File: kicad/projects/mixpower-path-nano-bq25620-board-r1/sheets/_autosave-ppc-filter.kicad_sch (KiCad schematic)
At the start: 5 parts, among them U4 TPS22917DBV

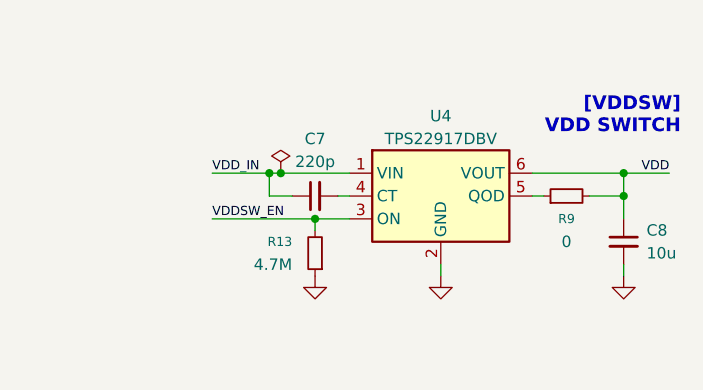
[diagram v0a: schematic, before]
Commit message: feat: implement the schematics and base project ideas/layout
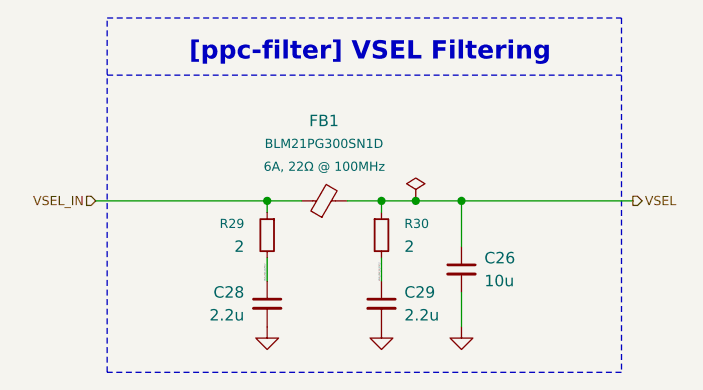
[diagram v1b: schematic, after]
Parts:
- removed C7: 220p, Capacitor_SMD:C_0402_1005Metric, symbol Device:C_Small
- removed C8: 10u, Capacitor_SMD:C_0402_1005Metric, symbol Device:C_Small
- removed R13: 4.7M, Resistor_SMD:R_0402_1005Metric, symbol Device:R_Small
- removed R9: 0, Resistor_SMD:R_0402_1005Metric, symbol Device:R_Small
- removed U4: TPS22917DBV, Package_TO_SOT_SMD:SOT-23-6, symbol Power_Management:TPS22917DBV
- added C26: 10u, Capacitor_SMD:C_0603_1608Metric, symbol Device:C_Small
- added C28, C29: 2.2u, Capacitor_SMD:C_0402_1005Metric, symbol Device:C_Small
- added FB1: BLM21PG300SN1D, Inductor_SMD:L_0805_2012Metric, symbol Device:FerriteBead_Small
- added R29, R30: 2, Resistor_SMD:R_0402_1005Metric, symbol Device:R_Small
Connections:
- net GND: now also C26.2, C28.2, C29.2
- new net VBUS_USBC_IN_POST_P: C29.1, R30.2
- new net VBUS_USBC_IN_PRE_P: C28.1, R29.2
- new net VSEL: C26.1, FB1.2, R30.1
- new net VSEL_IN: FB1.1, R29.1
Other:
- note added: "[ppc-filter] VSEL Filtering"
- note removed: "[VDDSW] VDD SWITCH"
